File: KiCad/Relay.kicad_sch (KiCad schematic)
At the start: 35 parts, among them J1 USB-C, J2 POWER, J3 Conn_01x10, U1 ESP32-PICO-MINI-02, U2 FT231XQ, U3 ISL89410, U4 ISL89410, U5 L96-M33, U6 LMR16006+FB, U7 AA, U8 QR

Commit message: Relay board
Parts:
- removed C2, C3: 33pF, RevK:C_0603, symbol Device:C
- removed D1: BAV99S, Package_TO_SOT_SMD:SOT-363_SC-70-6, symbol Diode:BAV99S
- removed J3: Conn_01x10, RevK:Molex_MiniSPOX_H10RA, symbol Connector_Generic:Conn_01x10
- removed R4: 100R, RevK:R_0603, symbol Device:R
- removed U5: L96-M33, RevK:L96-M33, symbol RevK:L96-M33
- added J10: O8, RevK:Molex_MiniSPOX_H2RA, symbol Connector_Generic:Conn_01x02
- added J3: O1, RevK:Molex_MiniSPOX_H2RA, symbol Connector_Generic:Conn_01x02
- added J4: O2, RevK:Molex_MiniSPOX_H2RA, symbol Connector_Generic:Conn_01x02
- added J5: O3, RevK:Molex_MiniSPOX_H2RA, symbol Connector_Generic:Conn_01x02
- added J6: O4, RevK:Molex_MiniSPOX_H2RA, symbol Connector_Generic:Conn_01x02
- added J7: O5, RevK:Molex_MiniSPOX_H2RA, symbol Connector_Generic:Conn_01x02
- added J8: O6, RevK:Molex_MiniSPOX_H2RA, symbol Connector_Generic:Conn_01x02
- added J9: O7, RevK:Molex_MiniSPOX_H2RA, symbol Connector_Generic:Conn_01x02
- added R6: 27R, RevK:R_0603, symbol Device:R
- added U4, U6: ISL89410, Package_SO:SO-8_3.9x4.9mm_P1.27mm, symbol Driver_FET:EL7202CN
- R7: value 100R -> 27R
- renumbered C4 to C2, C5 to C3, C6 to C4, D2 to D1, D3 to D2, D4 to D3, R5 to R4, R6 to R5, U4 to U5, U6 to U7, U7 to U8, U8 to U9
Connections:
- net FAULT is gone; now on net D+: R7.1
- net GPSRX is gone; now on net OUT2: U1.13 (IO33)
- net +12V: now also U4.6 (V+), U6.6 (V+)
- net B: now also U1.35 (IO21); no longer U1.34 (IO22)
- net D+: no longer J1.A6 (D+), J1.B6 (D+)
- net D-: now also R6.2; no longer J1.A7 (D-), J1.B7 (D-)
- net G: now also U1.33 (IO19); no longer U1.35 (IO21)
- net GND: now also J10.1 (Pin_1), J3.1 (Pin_1), J4.1 (Pin_1), J5.1 (Pin_1), J6.1 (Pin_1), J7.1 (Pin_1), J8.1 (Pin_1), J9.1 (Pin_1), U4.3 (GND), U6.3 (GND)
- net OUT1: now also U1.12 (IO32); no longer U1.18 (IO14)
- net OUT2: no longer U1.20 (IO13)
- net OUT3: now also U1.16 (IO26); no longer U1.21 (IO15)
- net OUT4: now also U1.15 (IO25); no longer U1.28 (IO8)
- net R: now also U1.34 (IO22); no longer U1.33 (IO19)
- net OUT5: now reaches U1.24 (IO4)
- net OUT5: now also U4.4 (IN_B)
- net BELL renamed O1
- net O1: now also J3.2 (Pin_2)
- net ENGHOLD renamed O3
- net O3: now also J5.2 (Pin_2)
- net GPSTICK: no longer names the net of U1.9 (I34)
- net GPSTX: no longer names the net of U1.10 (I35)
- net IN1 renamed OUT8
- net OUT8: now also U6.2 (IN_A)
- net IN2: no longer names the net of R7.2
- net IN2: now also J1.A6 (D+), J1.B6 (D+); no longer U1.26 (IO20)
- net STB renamed O2
- net O2: now also J4.2 (Pin_2)
- net ~{BACKLIGHT} renamed O4
- net O4: now also J6.2 (Pin_2)
- new net: J1.A7 (D-), J1.B7 (D-), R6.1
- new net O5: J7.2 (Pin_2), U4.5 (OUT_B)
- new net O6: J8.2 (Pin_2), U4.7 (OUT_A)
- new net O7: J9.2 (Pin_2), U6.5 (OUT_B)
- new net O8: J10.2 (Pin_2), U6.7 (OUT_A)
- new net OUT6: U1.26 (IO20), U4.2 (IN_A)
- new net OUT7: U1.28 (IO8), U6.4 (IN_B)
- no-connect marks 26 -> 16
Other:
- note removed: "Pinout matches Pyronix Deltabell"

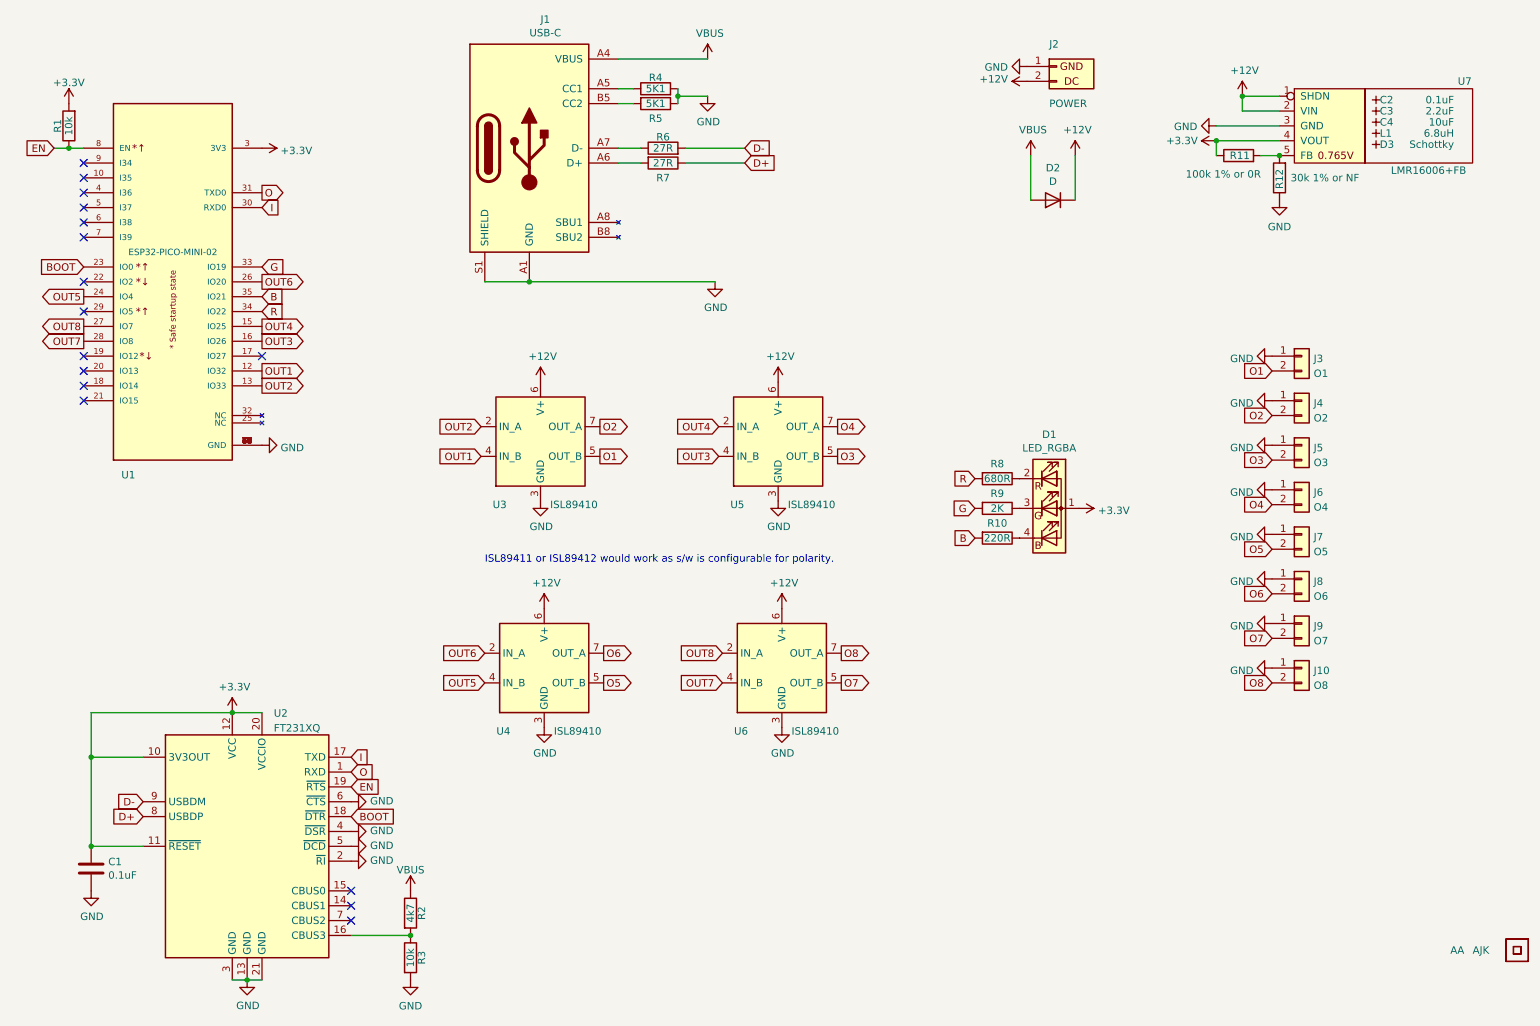
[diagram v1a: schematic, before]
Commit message: Added input
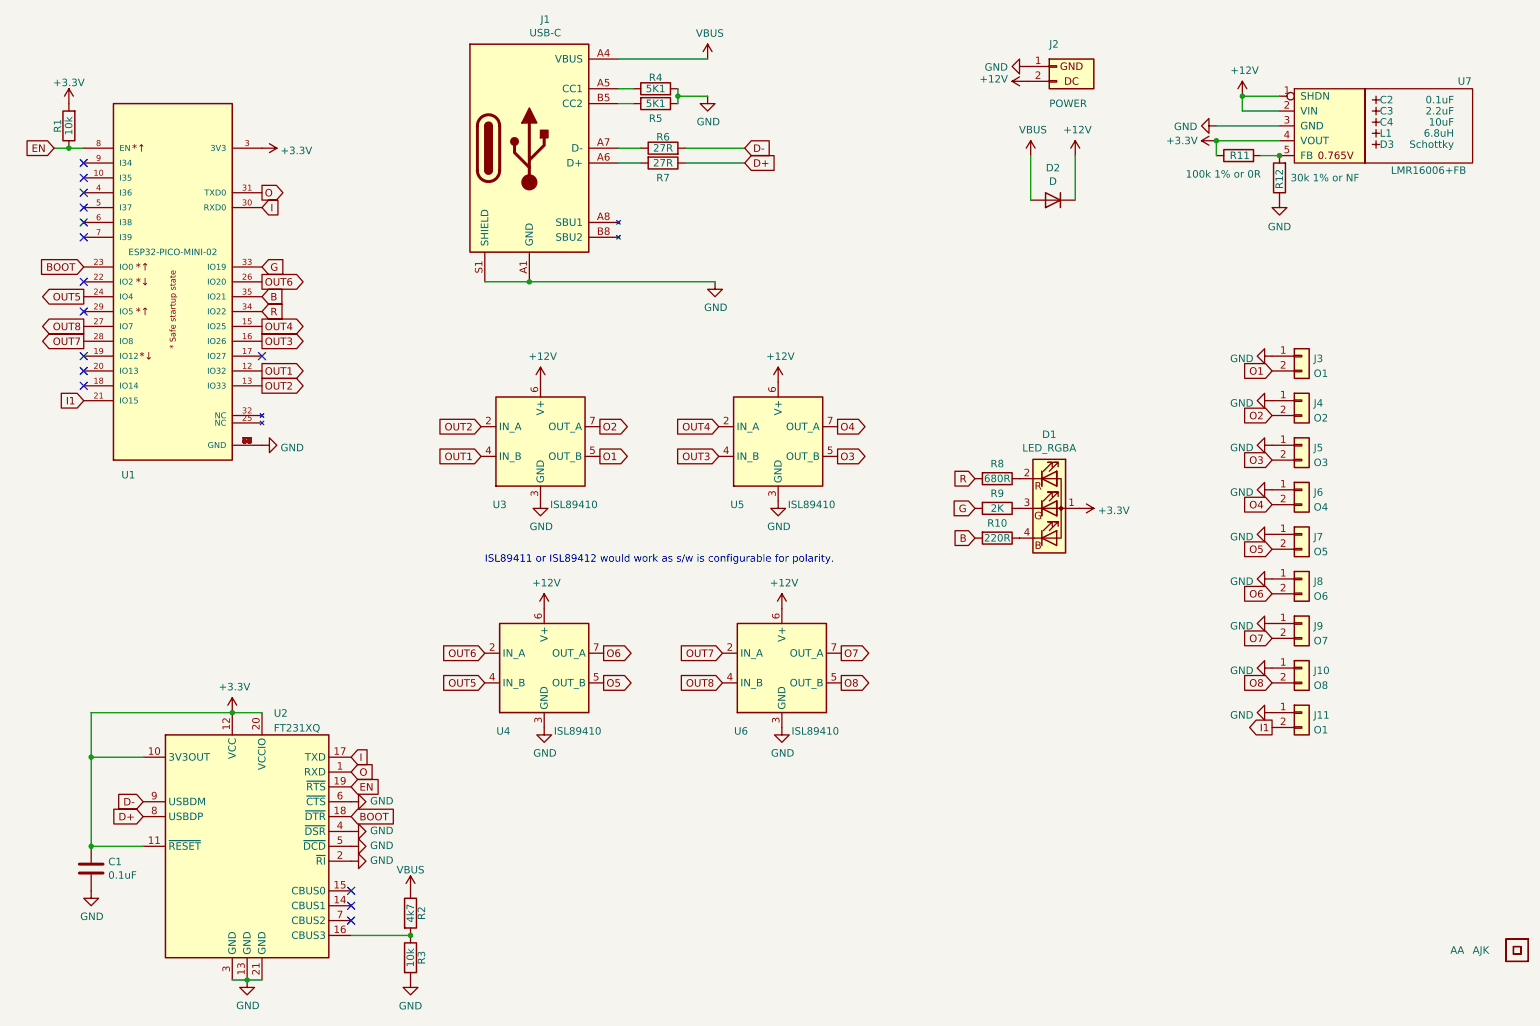
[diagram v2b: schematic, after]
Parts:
- added J11: O1, RevK:Molex_MiniSPOX_H2RA, symbol Connector_Generic:Conn_01x02
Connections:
- net GND: now also J11.1 (Pin_1)
- net O7: now also U6.7 (OUT_A); no longer U6.5 (OUT_B)
- net O8: now also U6.5 (OUT_B); no longer U6.7 (OUT_A)
- net OUT7: now also U6.2 (IN_A); no longer U6.4 (IN_B)
- net OUT8: now also U6.4 (IN_B); no longer U6.2 (IN_A)
- net I1: now reaches U1.21 (IO15)
- net I1: now also J11.2 (Pin_2)
- no-connect marks 16 -> 15
